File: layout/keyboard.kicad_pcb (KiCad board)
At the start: 2 copper layers, 271.5 x 95.3 mm, 113 parts, among them U1 ProMicro

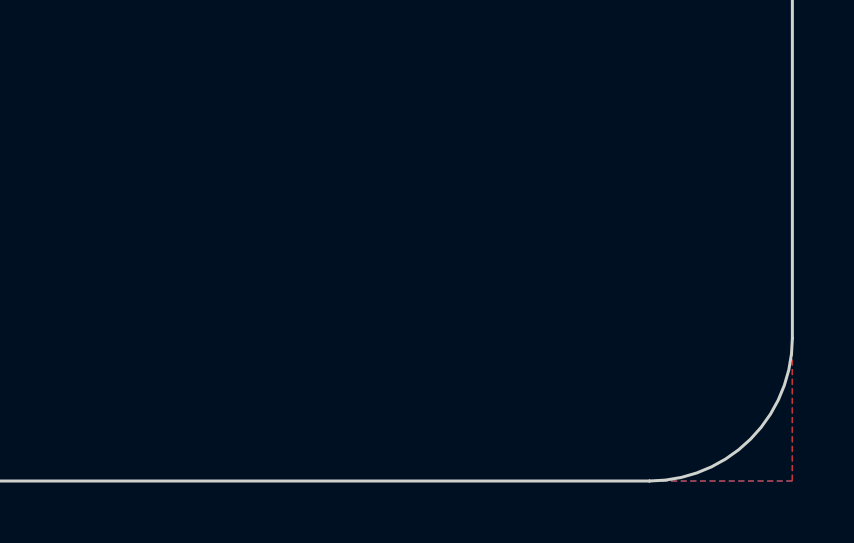
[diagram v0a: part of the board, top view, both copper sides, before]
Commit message: adding plate file and some silkscreens
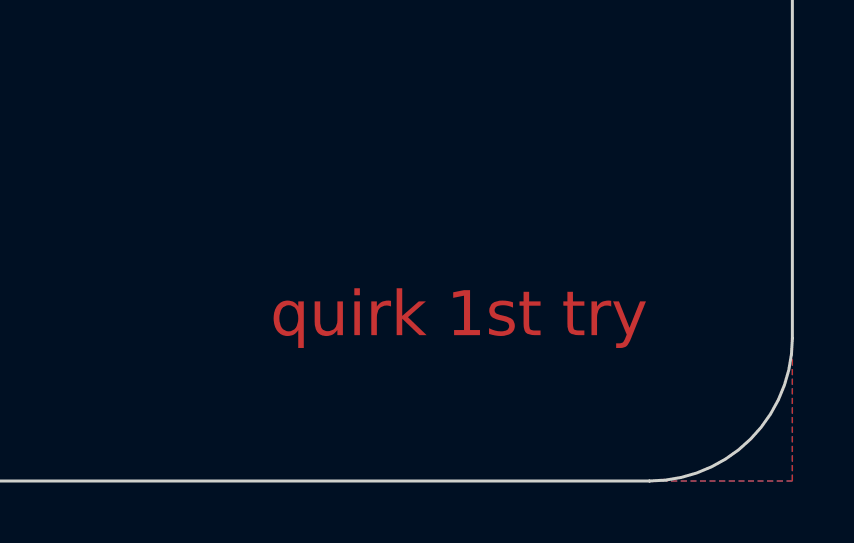
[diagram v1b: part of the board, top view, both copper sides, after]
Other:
- board text added: "quirk 1st try"

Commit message: Updating with latest stuff
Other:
- board text added: "quirk by astra jones 2021 r2"
- board text removed: "quirk 1st try"

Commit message: add 60% version
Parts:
- added G***: LOGO, silkscreens:meditate_nuki, B.Cu at (167.3, 69.9)
- added G***: LOGO, silkscreens:plate_corner_logo, B.Cu at (43.7, 107.2)
- added G***: LOGO, silkscreens:plate_corner_logo, F.Cu at (32.5, 99.2)
- added G***: LOGO, silkscreens:zest_nuki, F.Cu at (281.0, 78.6)
- added H1: Half Side Hole, acheron_MountingHoles:halfSideHole, F.Cu at (25.4, 80.4)
- added H4: Oval Mounting Hole, acheron_MountingHoles:MoutingHole_Oval_7mm_5.0x2.5mm, F.Cu at (214.9, 108.8)
- added H6: Half Side Hole, acheron_MountingHoles:halfSideHole, F.Cu at (308.4, 80.4)
- D_0, D_1, D_2, D_3, D_4, D_5, D_6, D_7, D_8, D_9, D_A1, D_ALT1, D_B1, D_BKSP1, D_BSLSH1, D_C1, D_CBRAC1, D_COMMA1, D_CTRL1, D_D1, D_DOT1, D_E1, D_EQUAL1, D_ESC1, D_F1, D_G1, D_H1, D_I1, D_J1, D_K1, D_L1, D_M1, D_MINUS1, D_N1, D_O1, D_OBRAC1, D_P1, D_Q1, D_QUOTE1, D_R1, D_S1, D_SEMIC1, D_SHIFT1, D_SLASH1, D_SPACE1, D_SPACE2, D_SUPER1, D_T1, D_TAB1, D_U1, D_V1, D_W1, D_X1, D_Y1, D_Z1, D_`1: footprint keyboard_parts:D_SOD123_axial -> Diode_SMD:D_SOD-123
- K_0, K_1, K_2, K_3, K_4, K_5, K_6, K_7, K_8, K_9, K_A1, K_B1, K_C1, K_CBRAC1, K_COMMA1, K_D1, K_DOT1, K_E1, K_EQUAL1, K_ESC1, K_F1, K_G1, K_H1, K_I1, K_J1, K_K1, K_L1, K_M1, K_MINUS1, K_N1, K_O1, K_OBRAC1, K_P1, K_Q1, K_QUOTE1, K_R1, K_S1, K_SEMIC1, K_SLASH1, K_T1, K_U1, K_V1, K_W1, K_X1, K_Y1, K_Z1, K_`1: footprint MX_Only:MXOnly-1U-NoLED -> MX_Only:MXOnly-1U-Hotswap
- K_ALT1, K_SUPER1: footprint MX_Only:MXOnly-1.25U-NoLED -> MX_Only:MXOnly-1.25U-Hotswap
- K_BKSP1: footprint MX_Only:MXOnly-2U-NoLED -> MX_Only:MXOnly-2U-Hotswap
- K_BSLSH1, K_TAB1: footprint MX_Only:MXOnly-1.5U-NoLED -> MX_Only:MXOnly-1.5U-Hotswap
- K_CTRL1: footprint MX_Only:MXOnly-1.75U-NoLED -> MX_Only:MXOnly-1U-Hotswap
- K_SHIFT1: footprint MX_Only:MXOnly-2.25U-NoLED -> MX_Only:MXOnly-2.25U-Hotswap
- K_SPACE1: footprint MX_Only:MXOnly-2.25U-ReversedStabilizers-NoLED -> MX_Only:MXOnly-2.75U-Hotswap-ReversedStabilizers
- K_SPACE2: footprint MX_Only:MXOnly-2.25U-ReversedStabilizers-NoLED -> MX_Only:MXOnly-2.25U-Hotswap-ReversedStabilizers
- U1: footprint Keebio-Parts:ArduinoProMicro -> Keebio-Parts:ArduinoProMicro-ZigZag
- moved U1 36.4 mm to (42.1, 39.7)
- moved K_BKSP1 29.0 mm to (289.5, 33.1)
- moved D_ALT1 29.0 mm to (128.4, 109.3)
- moved D_7 29.0 mm to (211.7, 33.1)
- moved D_L1 29.0 mm to (211.7, 52.1)
- moved K_7 29.0 mm to (203.8, 33.1)
- moved K_L1 29.0 mm to (203.8, 52.1)
- moved D_M1 29.0 mm to (211.7, 90.2)
- moved D_N1 29.0 mm to (211.7, 71.2)
- moved K_M1 29.0 mm to (203.8, 90.2)
- moved K_N1 29.0 mm to (203.8, 71.2)
- moved D_2 29.0 mm to (116.5, 33.1)
- moved D_CBRAC1 29.0 mm to (83.1, 109.3)
- moved D_ESC1 29.0 mm to (78.4, 33.0)
- moved D_W1 29.0 mm to (116.5, 52.1)
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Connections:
- U1 pad 1: col5 -> row1
- U1 pad 10: row2 -> row3
- U1 pad 11: row3 -> row4
- U1 pad 12: row4 -> Net-(U1-Pad12)
- U1 pad 13: col11 -> col6
- U1 pad 14: col10 -> col5
- U1 pad 15: col9 -> col4
- U1 pad 16: col8 -> col3
- U1 pad 17: col7 -> col2
- U1 pad 18: col6 -> col1
- U1 pad 19: row1 -> col0
- U1 pad 2: Net-(U1-Pad2) -> col7
- U1 pad 5: col4 -> col8
- U1 pad 6: col3 -> col9
- U1 pad 7: col2 -> col10
- U1 pad 8: col1 -> col11
- U1 pad 9: col0 -> row2
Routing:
- net row1: track 242.9 -> 305.0 mm, vias 0 -> 12
- net col11: track 306.7 -> 353.4 mm
- net row2: track 260.4 -> 298.3 mm, vias 0 -> 12
- net row4: track 271.3 -> 309.0 mm, vias 0 -> 8
- net row3: track 279.3 -> 312.4 mm, vias 0 -> 12
- net col5: track 227.1 -> 194.1 mm
- net row0: track 240.7 -> 271.8 mm, vias 0 -> 12
- net col4: track 174.7 -> 150.4 mm
- net col3: track 176.2 -> 152.6 mm
- net col2: track 156.6 -> 134.8 mm
- net col10: track 288.4 -> 310.0 mm
- net col8: track 233.2 -> 254.6 mm
- net col0: track 92.1 -> 71.4 mm, vias 1 -> 0
- net col1: track 136.6 -> 116.0 mm
- net col9: track 275.9 -> 293.8 mm
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- added copper zone on B.Cu, net (none)
- removed copper zone on B.Cu, net GND
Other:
- board size 271.5 x 95.3 mm -> 285 x 94.5 mm
- board text added: "astra jones 2021 // 60% r1"
- board text removed: "quirk by astra jones 2021 r2"
